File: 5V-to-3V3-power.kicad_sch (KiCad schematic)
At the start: 12 parts, among them J1 USB_C_Receptacle_USB2.0, U1 AMS1117-3.3

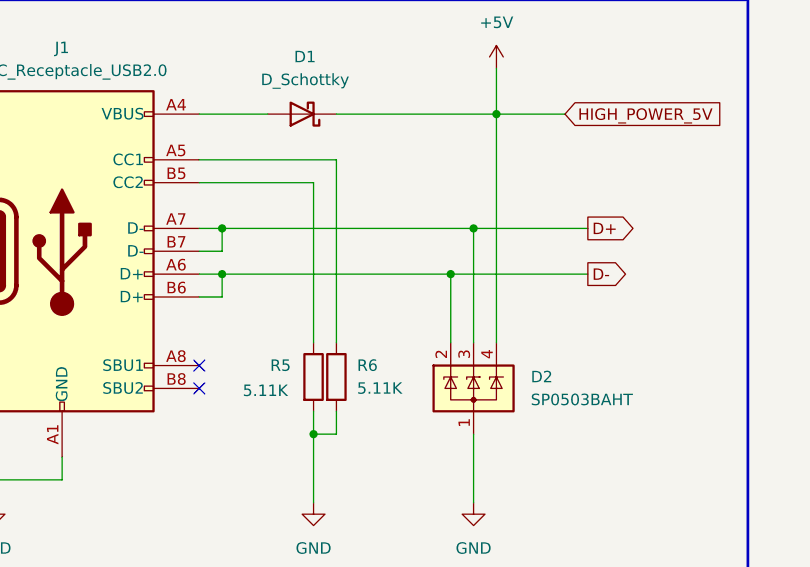
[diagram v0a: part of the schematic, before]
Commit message: ADD placement and rounting for ESP32-LED Driver
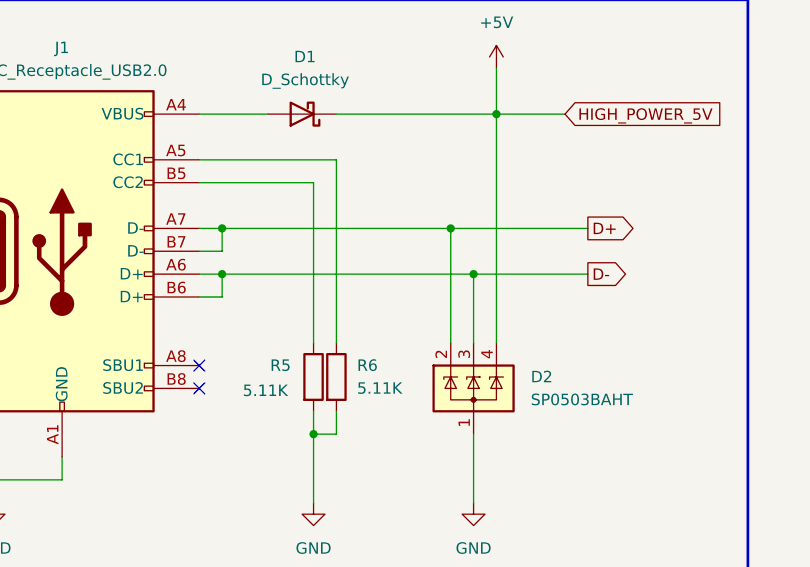
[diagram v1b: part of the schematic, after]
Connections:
- net D+: now also D2.2 (K); no longer D2.3 (K)
- net D-: now also D2.3 (K); no longer D2.2 (K)
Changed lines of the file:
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@@
   (junction (at 213.36 106.68) (diameter 0) (color 0 0 0 0)
   )
+  (junction (at 114.3 99.06) (diameter 0) (color 0 0 0 0)
+  )
+  (junction (at 111.76 93.98) (diameter 0) (color 0 0 0 0)
+  )
   (junction (at 193.04 66.04) (diameter 0) (color 0 0 0 0)
   )
@@
   (junction (at 208.28 88.9) (diameter 0) (color 0 0 0 0)
   )
-  (junction (at 114.3 93.98) (diameter 0) (color 0 0 0 0)
-  )
   (junction (at 223.52 66.04) (diameter 0) (color 0 0 0 0)
   )
   (junction (at 193.04 106.68) (diameter 0) (color 0 0 0 0)
-  )
-  (junction (at 111.76 99.06) (diameter 0) (color 0 0 0 0)
   )
   (no_connect (at 83.82 111.76))
@@
     (stroke (width 0) (type default) (color 0 0 0 0))
   )
+  (wire (pts (xy 114.3 99.06) (xy 127 99.06))
+    (stroke (width 0) (type default) (color 0 0 0 0))
+  )
   (wire (pts (xy 208.28 91.44) (xy 208.28 88.9))
     (stroke (width 0) (type default) (color 0 0 0 0))
@@
     (stroke (width 0.3) (type default) (color 25 28 255 1))
   )
-  (wire (pts (xy 86.36 93.98) (xy 114.3 93.98))
+  (wire (pts (xy 86.36 93.98) (xy 111.76 93.98))
     (stroke (width 0) (type default) (color 0 0 0 0))
   )
@@
     (stroke (width 0) (type default) (color 0 0 0 0))
   )
+  (wire (pts (xy 114.3 99.06) (xy 114.3 106.68))
+    (stroke (width 0) (type default) (color 0 0 0 0))
+  )
   (wire (pts (xy 60.96 121.92) (xy 60.96 124.46))
     (stroke (width 0) (type default) (color 0 0 0 0))
@@
     (stroke (width 0) (type default) (color 0 0 0 0))
   )
-  (wire (pts (xy 111.76 99.06) (xy 111.76 106.68))
-    (stroke (width 0) (type default) (color 0 0 0 0))
-  )
-  (wire (pts (xy 114.3 93.98) (xy 114.3 106.68))
+  (wire (pts (xy 111.76 93.98) (xy 111.76 106.68))
     (stroke (width 0) (type default) (color 0 0 0 0))
   )
@@
     (stroke (width 0) (type default) (color 0 0 0 0))
   )
-  (wire (pts (xy 86.36 99.06) (xy 111.76 99.06))
+  (wire (pts (xy 86.36 99.06) (xy 114.3 99.06))
     (stroke (width 0) (type default) (color 0 0 0 0))
   )
@@
     (stroke (width 0) (type default) (color 0 0 0 0))
   )
-  (wire (pts (xy 114.3 93.98) (xy 127 93.98))
-    (stroke (width 0) (type default) (color 0 0 0 0))
-  )
   (wire (pts (xy 86.36 99.06) (xy 83.82 99.06))
     (stroke (width 0) (type default) (color 0 0 0 0))
@@
     (stroke (width 0) (type default) (color 0 0 0 0))
   )
-  (wire (pts (xy 111.76 99.06) (xy 127 99.06))
-    (stroke (width 0) (type default) (color 0 0 0 0))
-  )
+  (wire (pts (xy 111.76 93.98) (xy 127 93.98))
+    (stroke (width 0) (type default) (color 0 0 0 0))
+  )
